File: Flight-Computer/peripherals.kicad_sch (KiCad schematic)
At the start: 36 parts, among them P10 Micro_SD_Card, P8 USB, P9 1984659, Q5 QS5U17TR, Q6 QS5U17TR, U10 TS391IYLT, U11 TS391IYLT, U6 SST25VF040B-50-4I-S2AE-T, U7 RFM95W-868S2, U8 CP2102-GMR(QFN28), U9 TS391IYLT

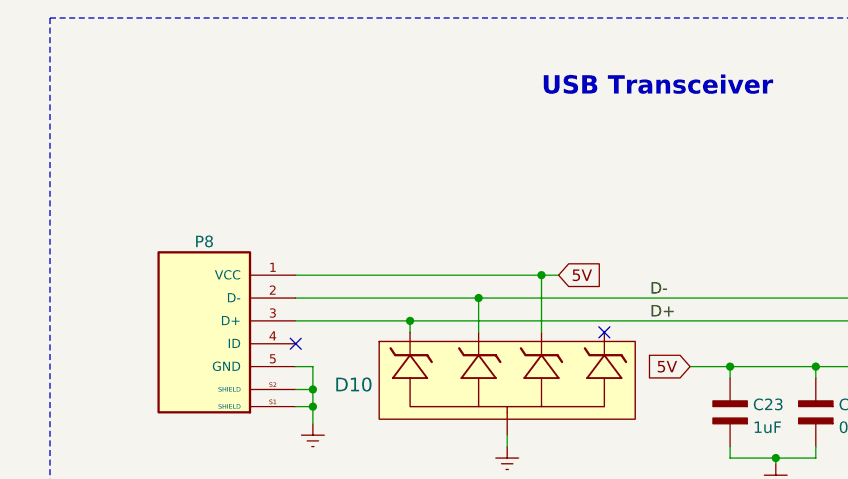
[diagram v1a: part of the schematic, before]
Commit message: Ports
Added 2 UART ports for connectivity, expanded board
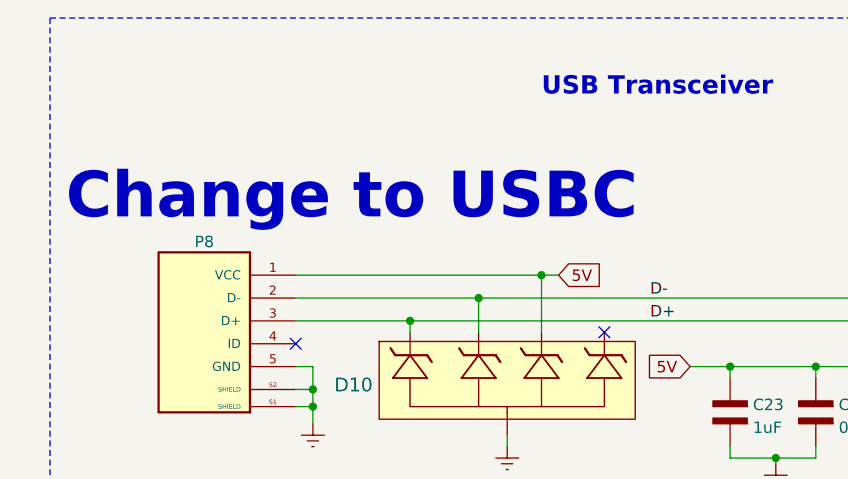
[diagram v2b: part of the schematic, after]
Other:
- note added: "Change to USBC"
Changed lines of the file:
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@@
+		)
+	)
+	(text "Change to USBC\n"
+		(exclude_from_sim no)
+		(at 51.308 38.354 0)
+		(effects
+			(font
+				(size 5.08 5.08)
+				(thickness 1.016)
+				(bold yes)
+			)
 		)
 	)

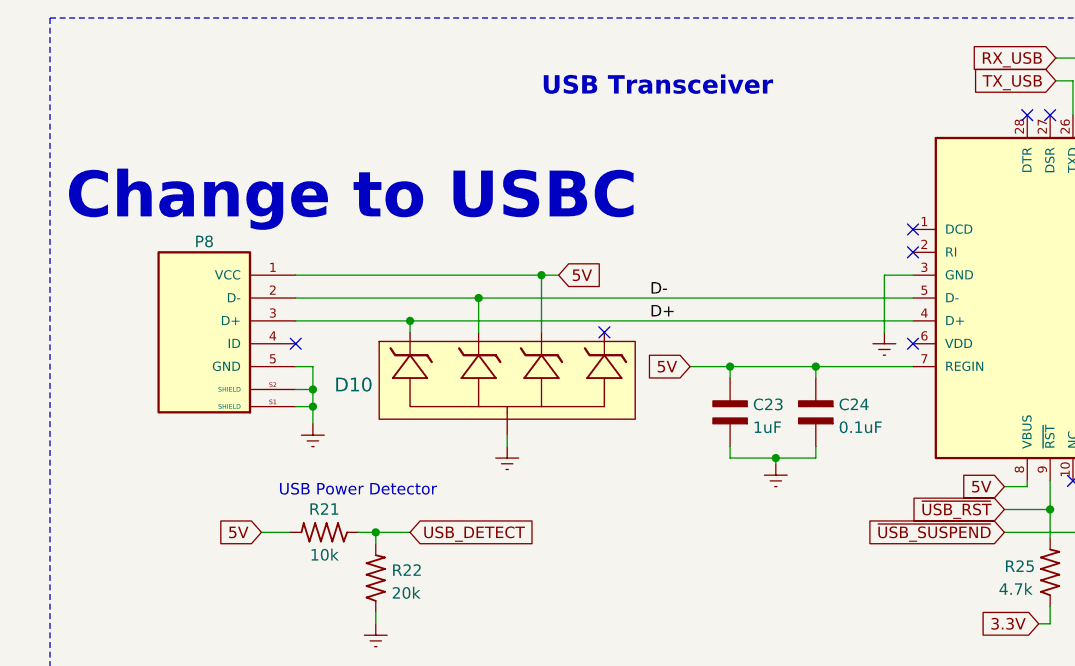
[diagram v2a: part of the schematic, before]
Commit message: most up to date rev 2.5 files
third connector (where micro sd used to be) does not have tx3 pins connected (pin outs needed in order to wire)
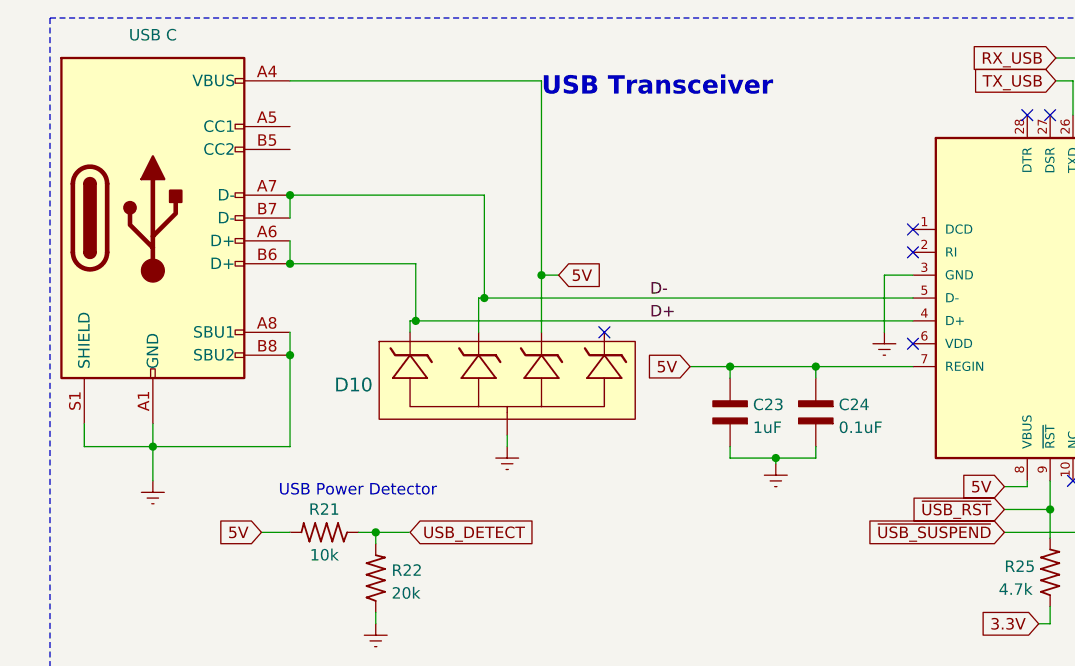
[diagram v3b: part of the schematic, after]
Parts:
- removed P8: USB, Flight-Computer:10118194-0001LF, symbol Flight-Computer:USB
- added J6: USB C, symbol Connector:USB_C_Receptacle_USB2.0_16P
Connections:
- net 5V: now also J6.A4 (VBUS), J6.A9 (VBUS), J6.B4 (VBUS), J6.B9 (VBUS)
- net D+: now also J6.A6 (D+), J6.B6 (D+)
- net D-: now also J6.A7 (D-), J6.B7 (D-)
- net Earth: now also J6.A1 (GND), J6.A12 (GND), J6.A8 (SBU1), J6.B1 (GND), J6.B12 (GND), J6.B8 (SBU2), J6.S1 (SHIELD)
- no-connect marks 21 -> 20
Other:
- note removed: "Change to USBC"
